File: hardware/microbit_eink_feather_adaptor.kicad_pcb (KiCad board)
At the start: 2 copper layers, 50.8 x 22.9 mm, 6 parts, among them J1 feather long, J2 feather short

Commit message: Update project from KiCARd 5 to 6.
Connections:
- net /~RST renamed /~{RST}
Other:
- net class Default removed
- board text added: "~{RST}"
- board text removed: "~RST"

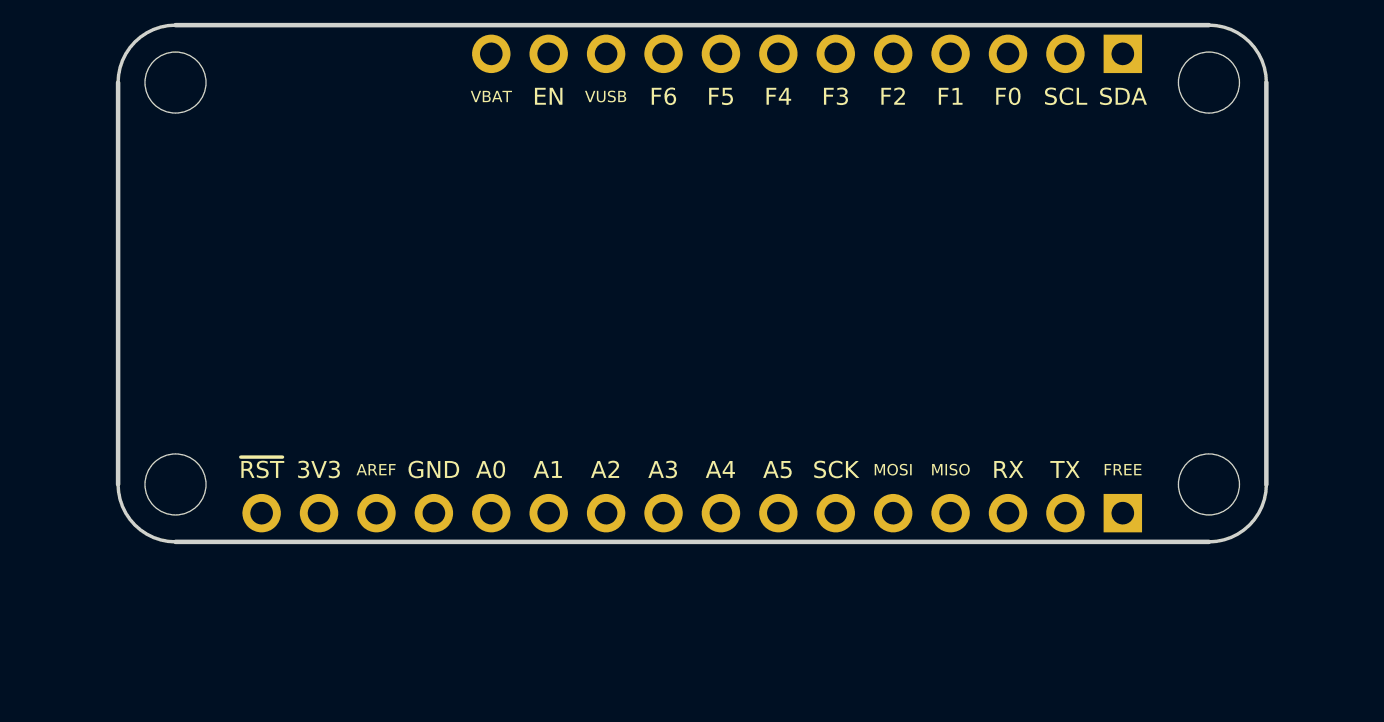
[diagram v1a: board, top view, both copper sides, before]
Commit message: Add micro:bit edge connector to project.
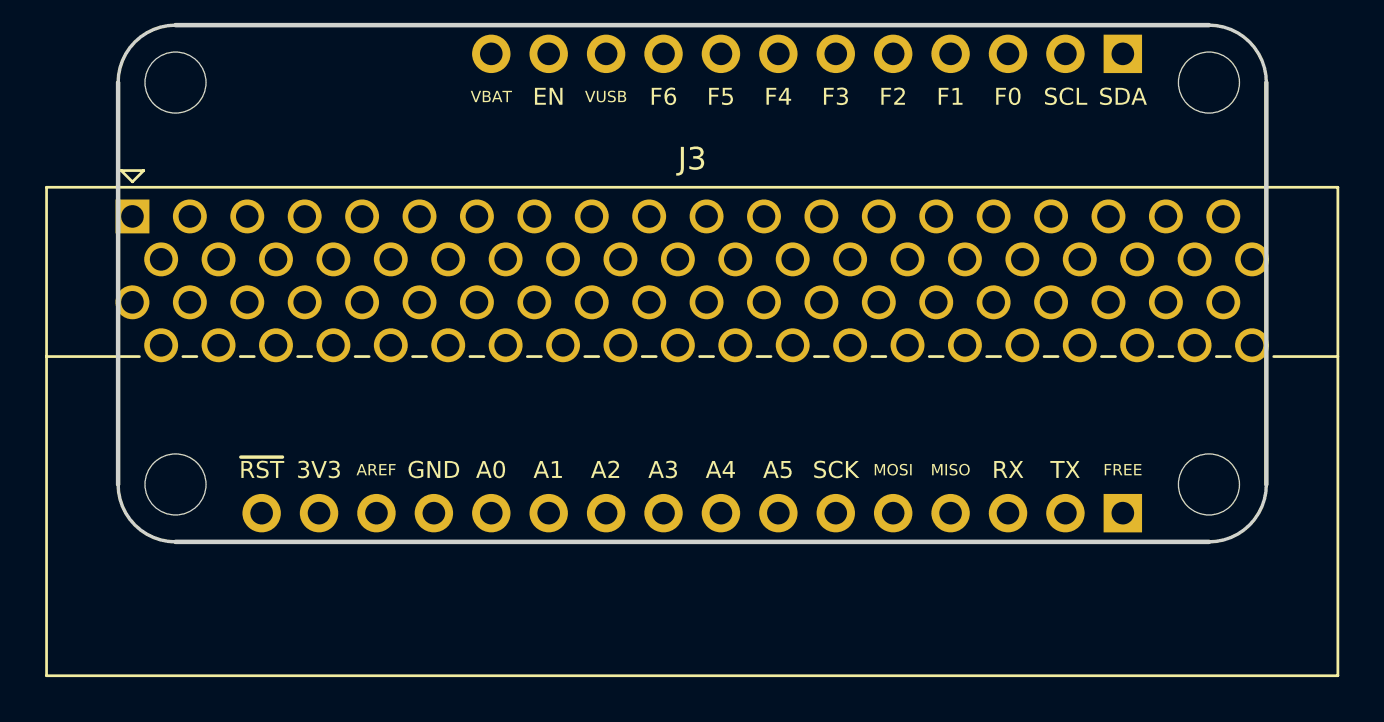
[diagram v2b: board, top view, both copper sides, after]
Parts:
- added J3: microbit_edge_connector, Connector_PCBEdge:4UCON_10156_2x40_P1.27mm_Socket_Horizontal, F.Cu at (26.0, 33.9)

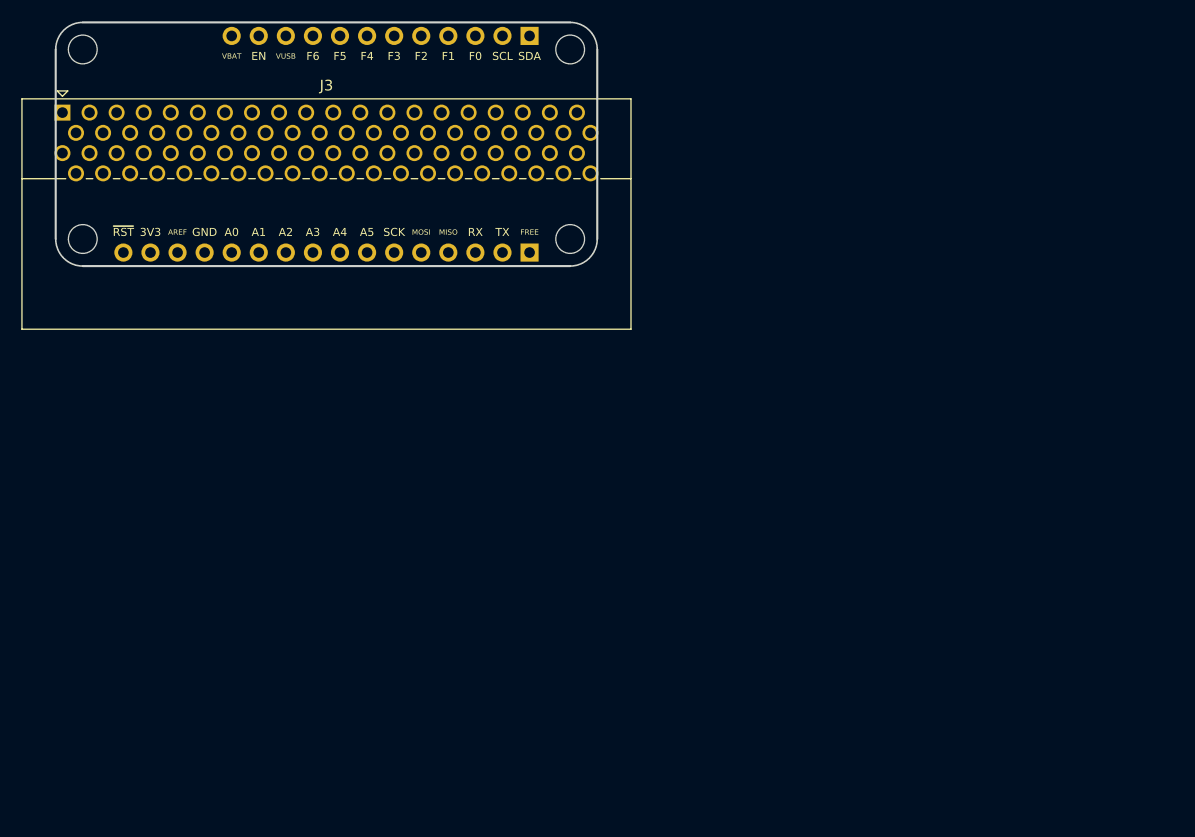
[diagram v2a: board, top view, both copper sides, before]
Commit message: Increase board size, place edge connector, and route 3V, GND, and SPI pins.
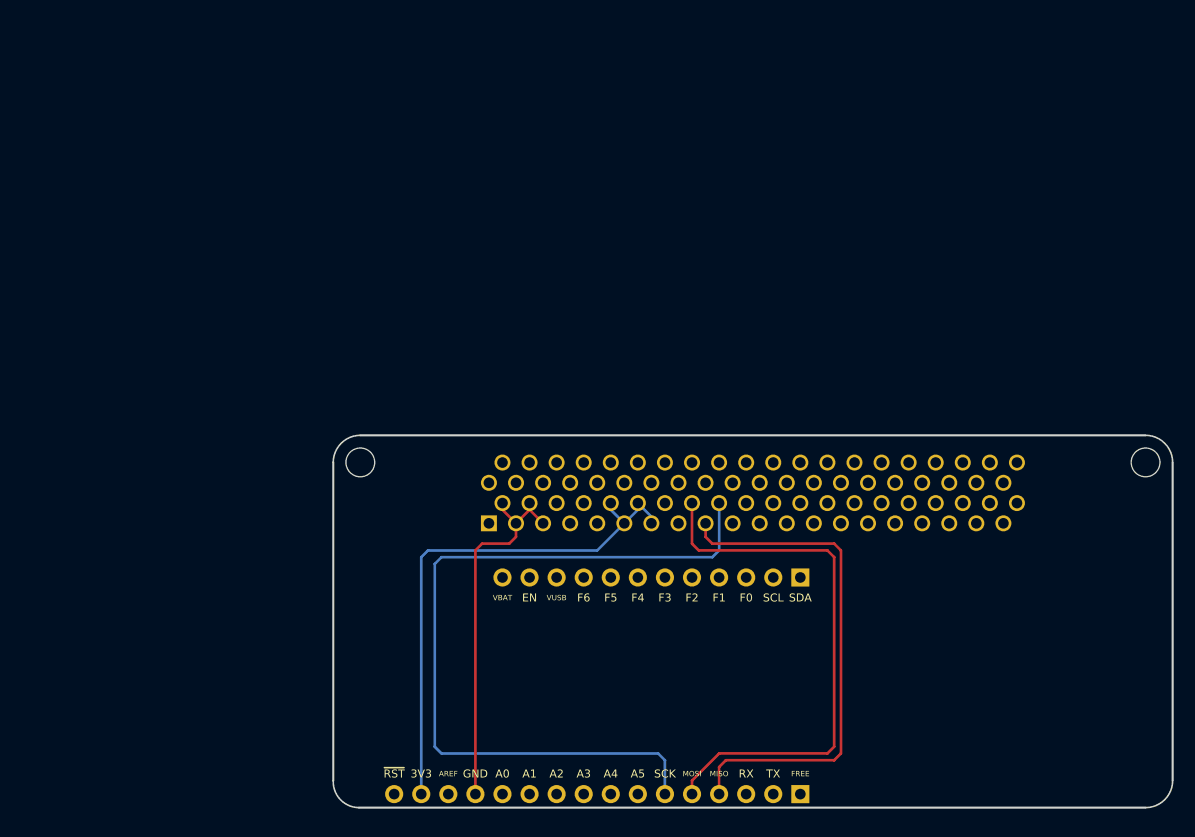
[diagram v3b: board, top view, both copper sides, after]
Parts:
- removed the REF** at (27.9, 45.7)
- removed the REF** at (73.7, 45.7)
- J3: moved to B.Cu
- moved REF** 66.4 mm to (127.6, 66.7)
- moved J1 56.8 mm to (95.2, 97.8)
- moved J2 56.8 mm to (95.2, 77.5)
- moved J3 55.5 mm to (66.0, 72.4)
- moved REF** 46.7 mm to (54.0, 66.7)
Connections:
- J3 pad 19: unconnected-(J3-Pad19) -> +3V3
- J3 pad 21: unconnected-(J3-Pad21) -> +3V3
- J3 pad 23: unconnected-(J3-Pad23) -> +3V3
- J3 pad 25: unconnected-(J3-Pad25) -> +3V3
- J3 pad 3: unconnected-(J3-Pad3) -> GND
- J3 pad 31: unconnected-(J3-Pad31) -> /MOSI
- J3 pad 33: unconnected-(J3-Pad33) -> /MISO
- J3 pad 35: unconnected-(J3-Pad35) -> /SCK
- J3 pad 5: unconnected-(J3-Pad5) -> GND
- J3 pad 7: unconnected-(J3-Pad7) -> GND
- J3 pad 75: unconnected-(J3-Pad75) -> /F4
- J3 pad 9: unconnected-(J3-Pad9) -> GND
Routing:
- net /SCK: track 0.00 -> 74.1 mm
- net /MOSI: track 0.00 -> 51.4 mm
- net +3V3: track 0.00 -> 49.9 mm
- net /MISO: track 0.00 -> 48.0 mm
- net GND: track 0.00 -> 35.1 mm
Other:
- board size 50.8 x 22.9 mm -> 78.7 x 34.9 mm

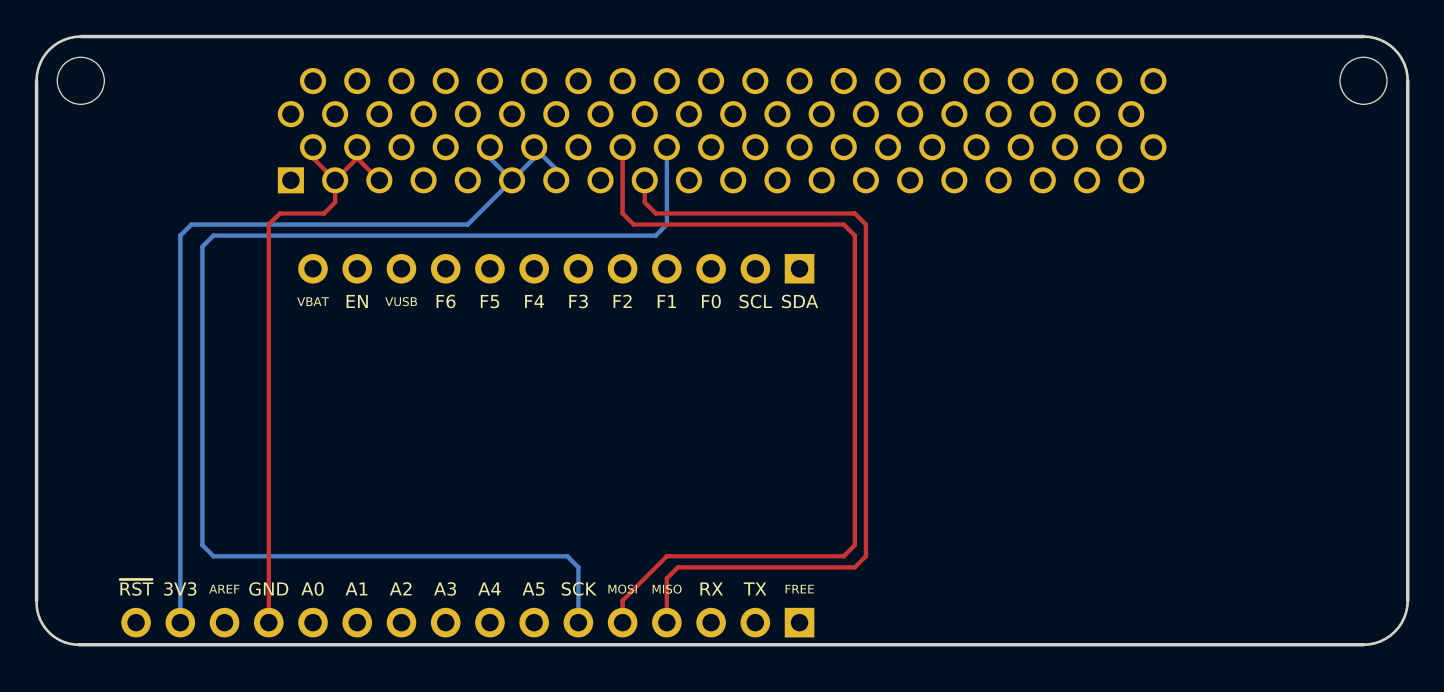
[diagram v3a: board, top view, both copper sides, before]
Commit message: Route all pins and complete initial version of board.
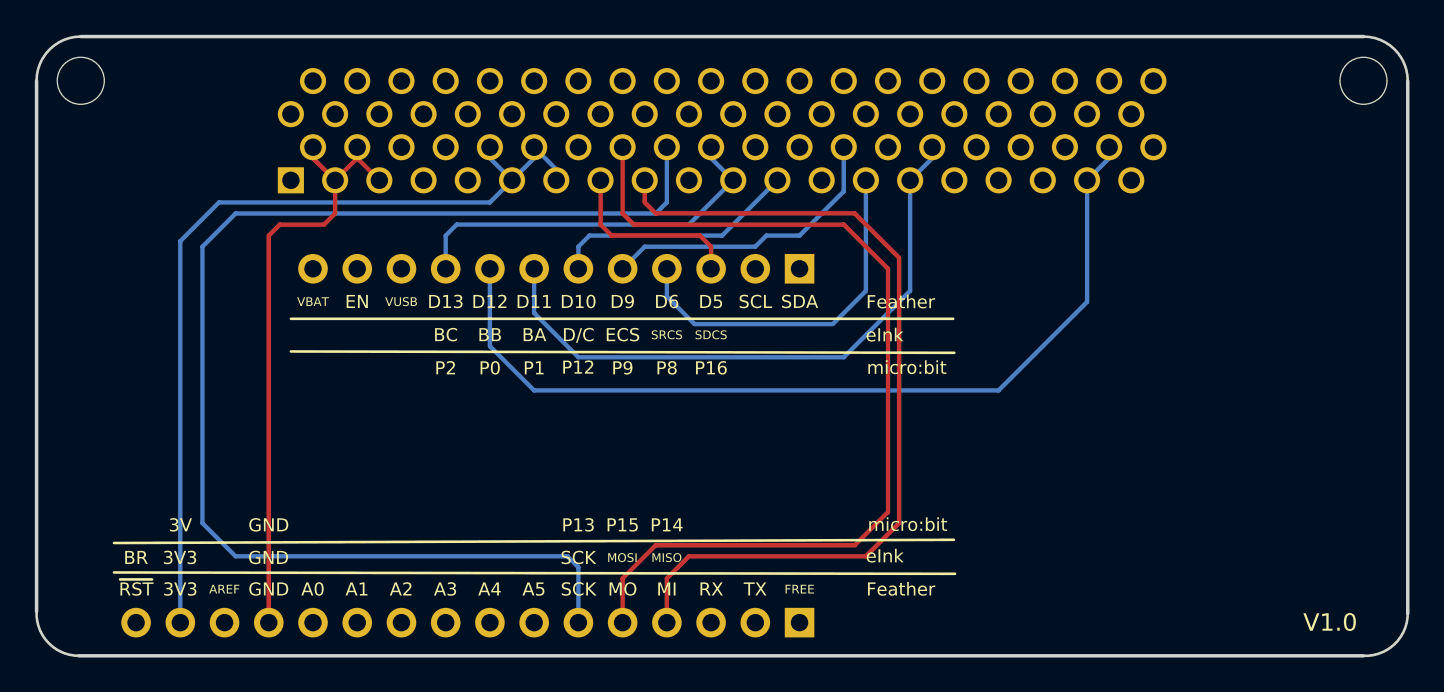
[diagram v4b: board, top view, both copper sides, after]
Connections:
- J2 pad 3: /F0 -> /D5
- J2 pad 4: /F1 -> /D6
- J2 pad 5: /F2 -> /D9
- J2 pad 6: /F3 -> /D10
- J2 pad 7: /F4 -> /D11
- J2 pad 8: /F5 -> /D12
- J2 pad 9: /F6 -> /D13
- J3 pad 29: unconnected-(J3-Pad29) -> /D5
- J3 pad 39: unconnected-(J3-Pad39) -> /D13
- J3 pad 41: unconnected-(J3-Pad41) -> /D13
- J3 pad 45: unconnected-(J3-Pad45) -> /D10
- J3 pad 51: unconnected-(J3-Pad51) -> /D9
- J3 pad 53: unconnected-(J3-Pad53) -> /D6
- J3 pad 57: unconnected-(J3-Pad57) -> /D11
- J3 pad 59: unconnected-(J3-Pad59) -> /D11
- J3 pad 73: unconnected-(J3-Pad73) -> /D12
- J3 pad 75: /F4 -> /D12
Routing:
- net /D12: track 0.00 -> 51.3 mm
- net /D11: track 0.00 -> 35.5 mm
- net /D13: track 0.00 -> 22.2 mm
- net /D6: track 0.00 -> 20.8 mm
- net /D9: track 0.00 -> 17.1 mm
- net /D10: track 0.00 -> 14.3 mm
- net /D5: track 0.00 -> 10.7 mm
- net /MOSI: track 51.4 -> 53.7 mm
- net /MISO: track 48.0 -> 49.6 mm
- net /SCK: track 74.1 -> 72.6 mm
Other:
- board size 78.7 x 34.9 mm -> 78.7 x 35.6 mm
- rule pad_to_mask_clearance: 0.051 -> 0
- board text added: "3V"
- board text added: "BA"
- board text added: "BB"
- board text added: "BC"
- board text added: "BR"
- board text added: "D/C"
- board text added: "D10"
- board text added: "D11"
- board text added: "D12"
- board text added: "D13"
- board text added: "D5"
- board text added: "D6"
- board text added: "D9"
- board text added: "ECS"
- board text added: "Feather"
- board text added: "JLCJLCJLCJLC"
- board text added: "MI"
- board text added: "MO"
- board text added: "P0"
- board text added: "P1"
- board text added: "P12"
- board text added: "P13"
- board text added: "P14"
- board text added: "P15"
- board text added: "P16"
- board text added: "P2"
- board text added: "P8"
- board text added: "P9"
- board text added: "SDCS"
- board text added: "SRCS"
- board text added: "V1.0"
- board text added: "eInk"
- board text added: "micro:bit"
- board text removed: "F0"
- board text removed: "F1"
- board text removed: "F2"
- board text removed: "F3"
- board text removed: "F4"
- board text removed: "F5"
- board text removed: "F6"

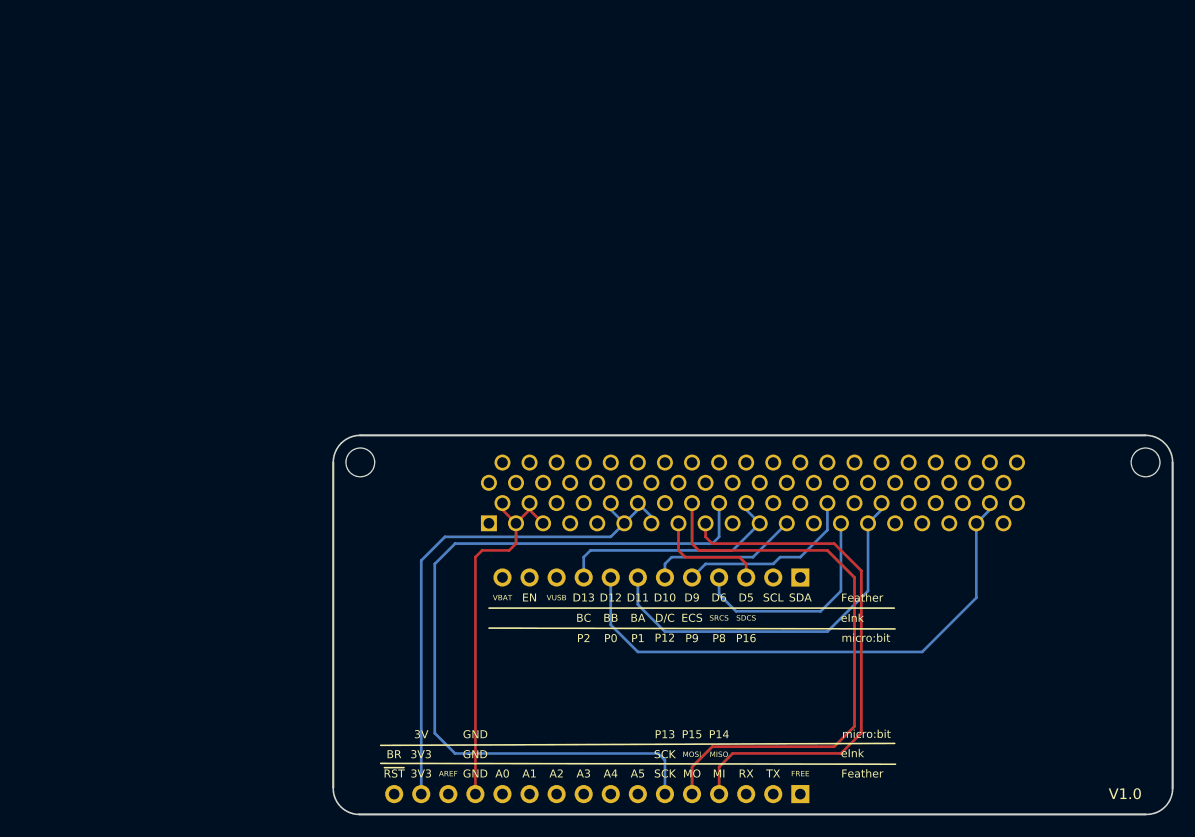
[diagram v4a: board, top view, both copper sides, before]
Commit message: pcb: Expand PCB to include butterfly hang hole.
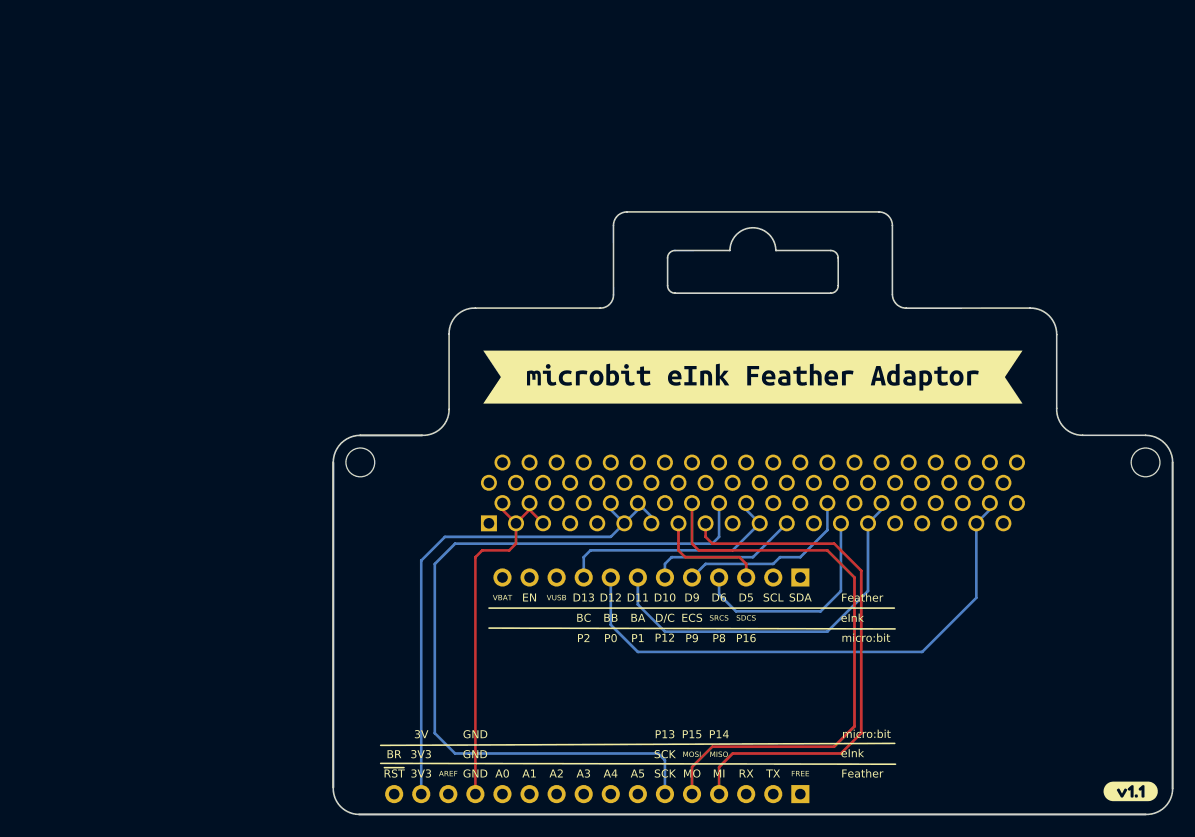
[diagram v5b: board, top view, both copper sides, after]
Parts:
- added kibuzzard-62B89D05: G***, kibuzzard-62B89D05, F.Cu at (126.2, 97.5)
- added kibuzzard-62B8B88C: G***, kibuzzard-62B8B88C, F.Cu at (90.8, 58.7)
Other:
- board size 78.7 x 35.6 mm -> 78.7 x 56.5 mm
- board text removed: "V1.0"
